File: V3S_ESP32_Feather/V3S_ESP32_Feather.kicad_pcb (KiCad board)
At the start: 2 copper layers, 30.5 x 50.8 mm, 82 parts, among them J1 USB_Micro, J10 UART, J2 PWM, J3 CAM, J4 I2C, J5 U.FL-R-SMT(01), J7 Micro_SD_Card_Det, J9 I2C, U1 V3S, U2 ADP322ACPZ-145-R7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

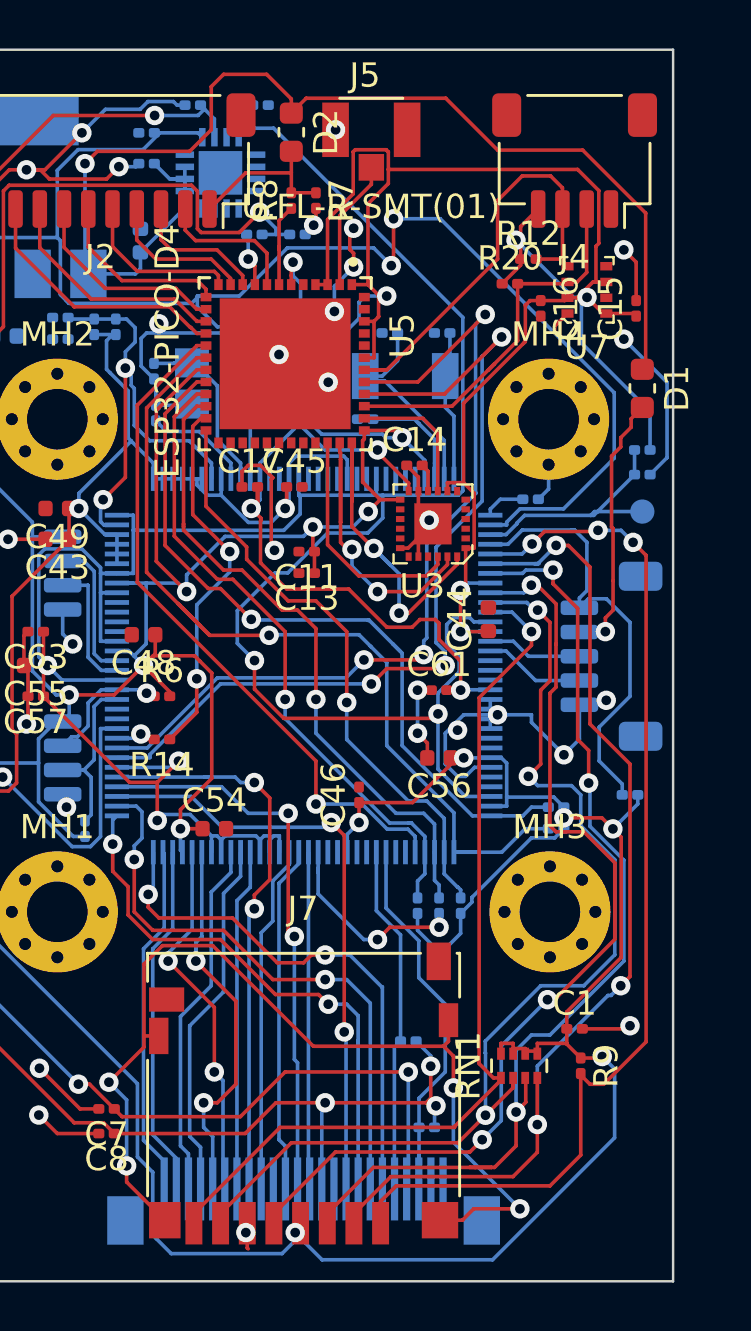
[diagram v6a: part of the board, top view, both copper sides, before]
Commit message: antenna cleanup, ground fixing almost done
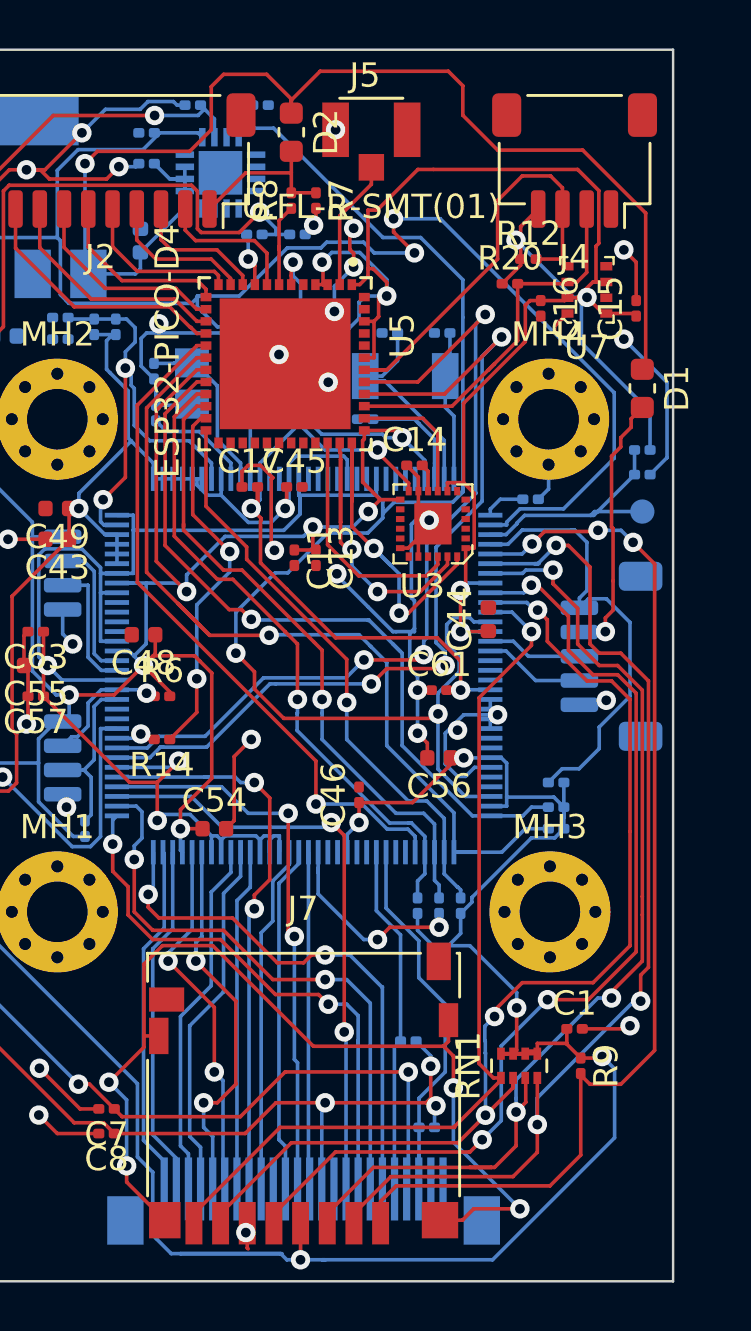
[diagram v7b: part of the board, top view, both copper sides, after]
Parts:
- moved R3 3.09 mm to (48.5, 49.3)
- moved C13 0.74 mm to (38.6, 40.0), turned to 270 degrees
- moved C11 0.57 mm to (37.7, 40.0), turned to 270 degrees
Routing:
- net GND: track 96.4 -> 106.9 mm, vias 29 -> 30
- net +3V3: track 267.1 -> 263.7 mm
- net +1V2: track 111.6 -> 114.7 mm
- net /PMIC Power Battery/VIN: track 49.6 -> 51.5 mm
- net /All V3s input output/PF2: track 40.0 -> 41.2 mm
- net /All V3s input output/PF4: track 42.5 -> 43.8 mm
- net /All V3s input output/PF3: track 41.8 -> 42.8 mm
- net /All V3s input output/PF5: track 44.4 -> 45.1 mm
- net /All V3s input output/SDIO1_DAT1: track 24.8 -> 24.1 mm

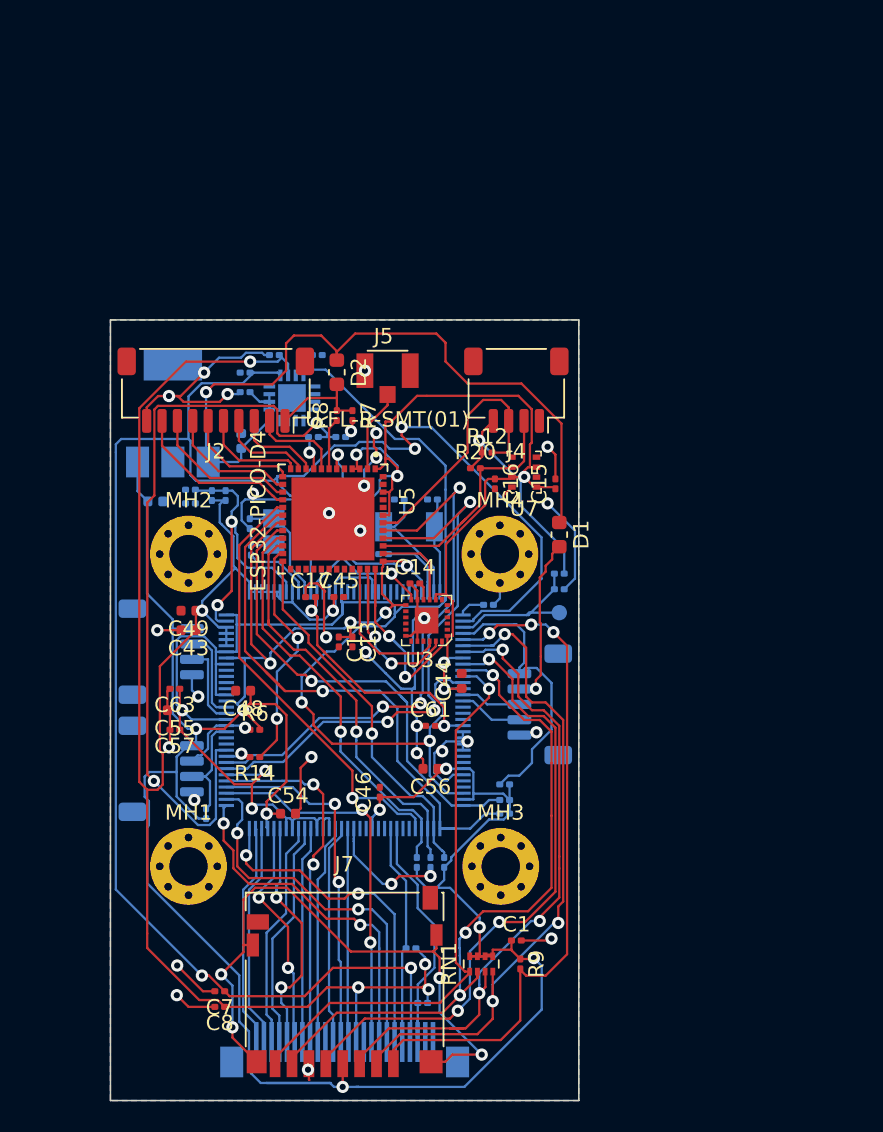
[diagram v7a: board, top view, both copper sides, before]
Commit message: routing done, started filling bom
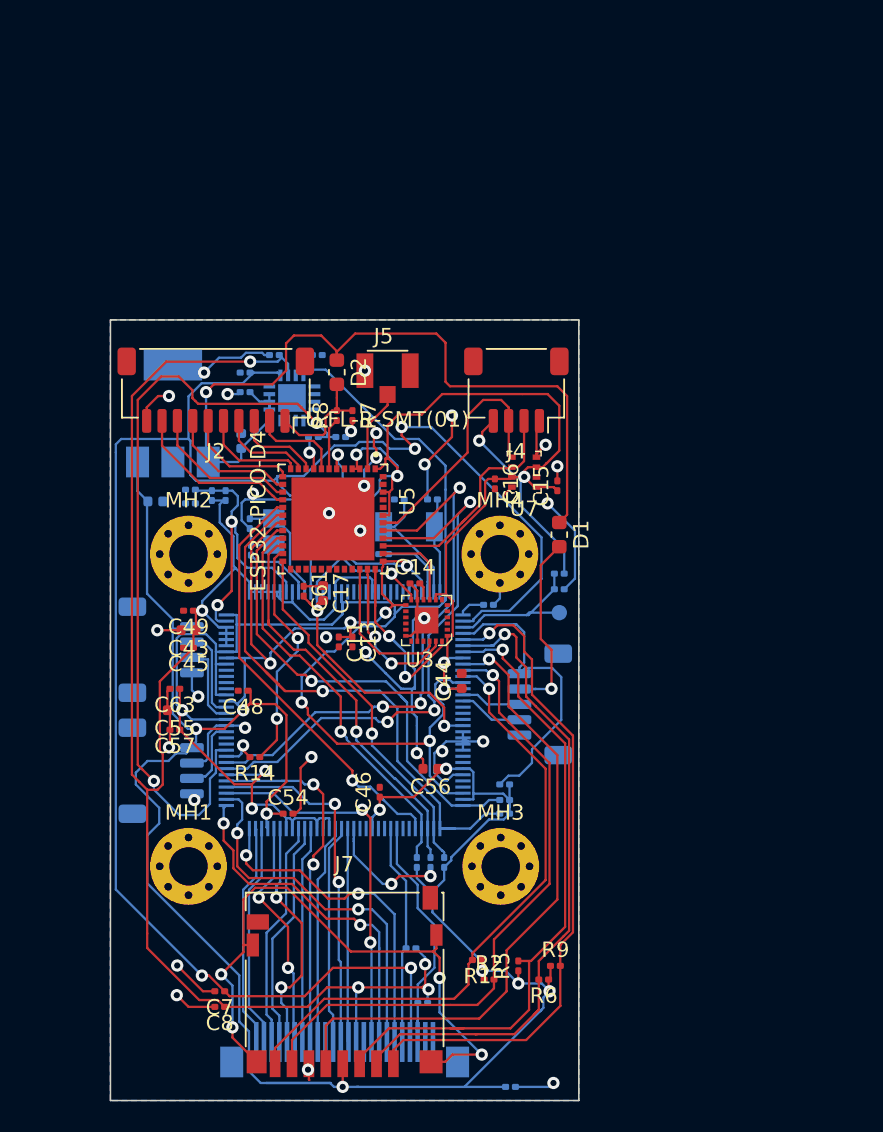
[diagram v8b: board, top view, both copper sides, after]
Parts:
- removed R12, R20: 1K, Resistor_SMD:R_0201_0603Metric
- removed RN1: 47K, Resistor_SMD:R_Array_Concave_4x0402
- added R1: 47K, Resistor_SMD:R_0201_0603Metric, F.Cu at (46.7, 60.7)
- added R2: 47K, Resistor_SMD:R_0201_0603Metric, F.Cu at (47.5, 62.0)
- C1: moved to B.Cu
- C17: footprint Capacitor_SMD:C_0201_0603Metric -> Capacitor_SMD:C_0402_1005Metric
- C48, C49, C54: footprint Capacitor_SMD:C_0402_1005Metric -> Capacitor_SMD:C_0201_0603Metric
- R10, R11, R29: value 2K -> 2K 1%
- R13, R14, R15, R16, R18, R19, R21: value 50K -> 47K
- R5: value 10K -> 47K; moved to F.Cu
- R6: value 10K -> 47K
- R7, R8: value R -> 47K
- moved R6 24.9 mm to (51.1, 62.0), turned to 180 degrees
- moved R5 22.6 mm to (49.4, 61.1)
- moved C61 12.0 mm to (35.4, 36.7), turned to 270 degrees
- moved C45 10.3 mm to (27.9, 40.4), turned to 180 degrees
- moved C1 9.53 mm to (48.9, 69.0)
- moved R9 2.29 mm to (51.8, 61.1), turned to 0 degrees
- moved C17 0.86 mm to (36.7, 36.8), turned to 270 degrees
- moved C15 0.18 mm to (51.9, 29.8)
- moved J10 0.13 mm to (26.2, 40.5)
- moved J9 0.13 mm to (26.2, 48.4)
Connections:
- J3 pad 1: (no net) -> /All V3s input output/STROBE
- J3 pad 10: (no net) -> Net-(J3-Pad10)
- J7 pad 10: (no net) -> Net-(J7-Pad10)
- J7 pad 9: (no net) -> Net-(J7-Pad9)
- R5 pad 2: Net-(J9-Pad2) -> /All V3s input output/PF3
- R6 pad 1: Net-(J9-Pad3) -> +3V3
- R6 pad 2: +3V3 -> /All V3s input output/PF4
- U1 pad 10: (no net) -> Net-(U1-Pad10)
- U1 pad 11: (no net) -> Net-(U1-Pad11)
- U1 pad 112: (no net) -> Net-(U1-Pad112)
- U1 pad 113: (no net) -> Net-(U1-Pad113)
- U1 pad 114: (no net) -> Net-(U1-Pad114)
- U1 pad 120: (no net) -> Net-(U1-Pad120)
- U1 pad 121: (no net) -> Net-(U1-Pad121)
- U1 pad 124: (no net) -> Net-(U1-Pad124)
- U1 pad 125: (no net) -> Net-(U1-Pad125)
- U1 pad 13: (no net) -> Net-(U1-Pad13)
- U1 pad 14: (no net) -> Net-(U1-Pad14)
- U1 pad 43: (no net) -> Net-(U1-Pad43)
- U1 pad 44: (no net) -> Net-(U1-Pad44)
- U1 pad 52: (no net) -> Net-(U1-Pad52)
- U1 pad 53: (no net) -> Net-(U1-Pad53)
- U1 pad 54: (no net) -> Net-(U1-Pad54)
- U1 pad 55: (no net) -> Net-(U1-Pad55)
- U1 pad 6: (no net) -> Net-(U1-Pad6)
- U1 pad 7: (no net) -> Net-(U1-Pad7)
- U1 pad 77: (no net) -> Net-(U1-Pad77)
- U1 pad 78: (no net) -> Net-(U1-Pad78)
- U1 pad 81: (no net) -> Net-(U1-Pad81)
- U1 pad 82: (no net) -> Net-(U1-Pad82)
- U1 pad 83: (no net) -> Net-(U1-Pad83)
- U1 pad 84: (no net) -> Net-(U1-Pad84)
- U1 pad 86: (no net) -> Net-(U1-Pad86)
- U1 pad 87: (no net) -> Net-(U1-Pad87)
- U1 pad 89: (no net) -> Net-(U1-Pad89)
- U1 pad 90: (no net) -> Net-(U1-Pad90)
- U1 pad 91: (no net) -> Net-(U1-Pad91)
- U1 pad 92: (no net) -> Net-(U1-Pad92)
- U2 pad 4: (no net) -> Net-(U2-Pad4)
- U2 pad 7: (no net) -> Net-(U2-Pad7)
- U3 pad 14: (no net) -> Net-(U3-Pad14)
- U3 pad 15: (no net) -> Net-(U3-Pad15)
- U3 pad 16: (no net) -> Net-(U3-Pad16)
- U3 pad 17: (no net) -> Net-(U3-Pad17)
- U3 pad 19: (no net) -> Net-(U3-Pad19)
- U3 pad 2: (no net) -> Net-(U3-Pad2)
- U3 pad 21: (no net) -> Net-(U3-Pad21)
- U3 pad 3: (no net) -> Net-(U3-Pad3)
- U3 pad 4: (no net) -> Net-(U3-Pad4)
- U3 pad 5: (no net) -> Net-(U3-Pad5)
- U3 pad 6: (no net) -> Net-(U3-Pad6)
- U3 pad 7: (no net) -> Net-(U3-Pad7)
- U5 pad 25: (no net) -> Net-(U5-Pad25)
- U5 pad 26: (no net) -> Net-(U5-Pad26)
- U5 pad 27: (no net) -> Net-(U5-Pad27)
- U5 pad 28: (no net) -> /WIFI, BT, RT/SD2
- U5 pad 29: (no net) -> /WIFI, BT, RT/SD3
- U5 pad 30: (no net) -> Net-(U5-Pad30)
- U5 pad 31: (no net) -> Net-(U5-Pad31)
- U5 pad 32: (no net) -> Net-(U5-Pad32)
- U5 pad 33: (no net) -> Net-(U5-Pad33)
- U5 pad 5: (no net) -> Net-(U5-Pad5)
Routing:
- net /All V3s input output/PF1: track 44.8 -> 41.7 mm, vias 3 -> 1
- net /All V3s input output/PF0: track 37.5 -> 40.3 mm
- net GND: track 106.9 -> 104.5 mm, vias 30 -> 31
- net /PMIC Power Battery/VIN: track 51.5 -> 53.9 mm
- net Net-(J9-Pad2): track 7.06 -> 4.73 mm
- net VBUS: track 11.0 -> 13.2 mm
- net /All V3s input output/PF5: track 45.1 -> 43.5 mm, vias 3 -> 1
- net /USB_ID: track 18.4 -> 19.6 mm
- net /WIFI, BT, RT/SCL: track 18.7 -> 17.6 mm
- net +BATT: track 6.72 -> 7.74 mm
- net /WIFI, BT, RT/EN: track 50.1 -> 51.1 mm
- net /WIFI, BT, RT/IO0_PULL: track 1.70 -> 2.59 mm
- net /All V3s input output/PF2: track 41.2 -> 42.1 mm, vias 3 -> 1
- net +3V3: track 263.7 -> 262.9 mm, vias 18 -> 19
- net /All V3s input output/SDIO1_CMD: track 27.0 -> 26.3 mm
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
